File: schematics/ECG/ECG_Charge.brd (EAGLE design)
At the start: 100 x 80 mm, 8 parts, among them IC1 MCP73832_SOT23-5, J1 USB_MICROC

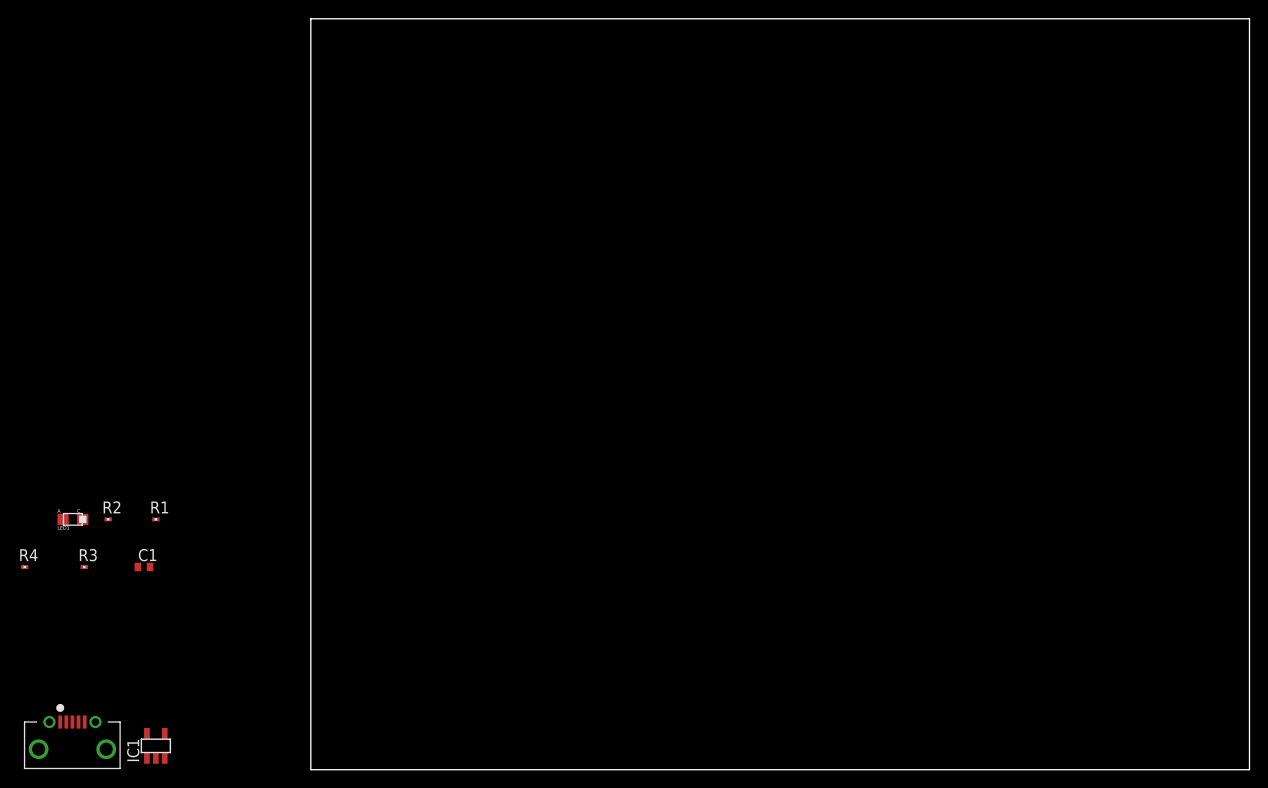
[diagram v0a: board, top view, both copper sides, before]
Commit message: changed usb to micro usb, placed components in board area
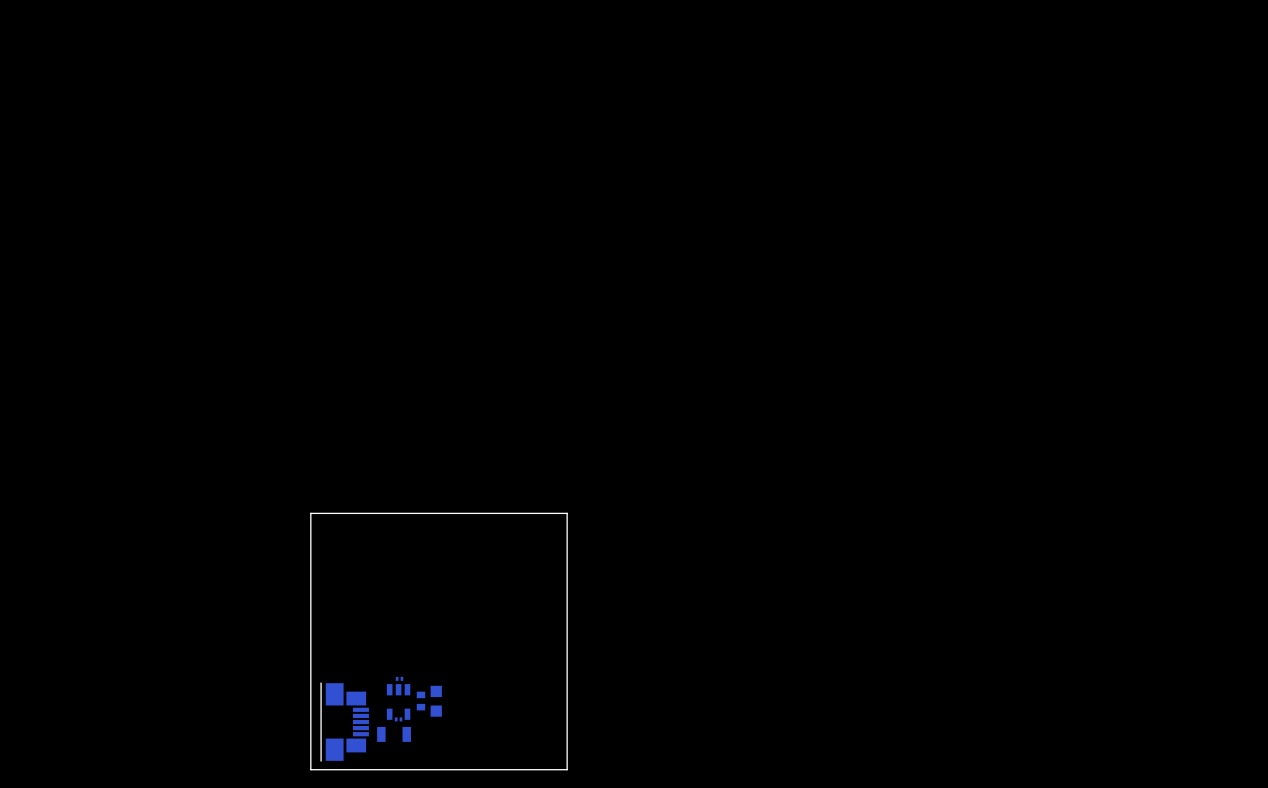
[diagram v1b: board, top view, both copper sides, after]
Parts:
- removed J1: USB_MICROC, KomodoOpenLab:USB_MICROB_FEMALE_RA_SMT
- removed R3, R4: 100K, rcl:R0201
- added FUSE: FUSE-MF_SERIES, bourns-fuse:1206
- added USBCONN: MOLEX-47346-0001, usb_con-update:MOLEX-47364-0001
- moved LED1 43.4 mm to (13.4, 7.24), flipped to the bottom, turned to 90 degrees
- moved R2 37.6 mm to (9.35, 5.36), flipped to the bottom
- moved C1 32.8 mm to (11.7, 7.32), flipped to the bottom, turned to 90 degrees
- moved R1 31.0 mm to (9.45, 9.68), flipped to the bottom, turned to 180 degrees
- moved IC1 26.3 mm to (9.35, 7.21), flipped to the bottom, turned to 180 degrees
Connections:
- removed net CHARGE_STAT: R3.1, R4.2
- removed net VIN: C1.1, IC1.4, J1.P$1, LED1.A
- new net VUSB: C1.1, FUSE.2, IC1.4, LED1.A
- new net VUSB_5V: FUSE.1, USBCONN.1
- net GND: now also USBCONN.5; no longer J1.P$5, R4.1
- net STAT: no longer R3.2
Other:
- board size 100 x 80 mm -> 27.3 x 27.3 mm
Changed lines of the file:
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@@
 <setting verticaltext="up"/>
 </settings>
-<grid distance="0.05" unitdist="inch" unit="inch" style="lines" multiple="1" display="no" altdistance="0.025" altunitdist="inch" altunit="inch"/>
+<grid distance="1" unitdist="mil" unit="mil" style="lines" multiple="1" display="no" altdistance="0.025" altunitdist="inch" altunit="inch"/>
 <layers>
 <layer number="1" name="Top" color="4" fill="1" visible="yes" active="yes"/>
+<layer number="2" name="Route2" color="1" fill="3" visible="no" active="no"/>
+<layer number="3" name="Route3" color="4" fill="3" visible="no" active="no"/>
+<layer number="14" name="Route14" color="1" fill="6" visible="no" active="no"/>
+<layer number="15" name="Route15" color="4" fill="6" visible="no" active="no"/>
 <layer number="16" name="Bottom" color="1" fill="1" visible="yes" active="yes"/>
 <layer number="17" name="Pads" color="2" fill="1" visible="yes" active="yes"/>
@@
 <board>
 <plain>
-<wire x1="0" y1="0" x2="100" y2="0" width="0" layer="20"/>
-<wire x1="100" y1="0" x2="100" y2="80" width="0" layer="20"/>
-<wire x1="100" y1="80" x2="0" y2="80" width="0" layer="20"/>
-<wire x1="0" y1="80" x2="0" y2="0" width="0" layer="20"/>
+<wire x1="0" y1="0" x2="27.305" y2="0" width="0" layer="20"/>
+<wire x1="27.305" y1="0" x2="27.305" y2="27.305" width="0" layer="20"/>
+<wire x1="27.305" y1="27.305" x2="0" y2="27.305" width="0" layer="20"/>
+<wire x1="0" y1="27.305" x2="0" y2="0" width="0" layer="20"/>
 </plain>
 <attributes>
@@
 </autorouter>
 <elements>
-<element name="J1" library="KomodoOpenLab" package="USB_MICROB_FEMALE_RA_SMT" value="USB_MICROC" x="-25.4" y="2.54">
-<attribute name="DIGIKEY" value="WM1399CT-ND" x="0" y="0" size="1.778" layer="27" display="off"/>
-<attribute name="PN" value="ZX62D-B-5PA8" x="0" y="0" size="1.778" layer="27" display="off"/>
-</element>
-<element name="IC1" library="KomodoOpenLab" package="SOT23-5" value="MCP73832_SOT23-5" x="-16.51" y="2.54"/>
-<element name="R2" library="rcl" package="R0201" value="10K" x="-21.59" y="26.67"/>
-<element name="C1" library="rcl" package="C0402" value="4.7uF" x="-17.78" y="21.59"/>
-<element name="R3" library="rcl" package="R0201" value="100K" x="-24.13" y="21.59"/>
-<element name="R4" library="rcl" package="R0201" value="100K" x="-30.48" y="21.59"/>
-<element name="LED1" library="LITEON" package="SMT_LED_0805" value="LED_SMT_0805" x="-25.4" y="26.67"/>
-<element name="R1" library="rcl" package="R0201" value="470" x="-16.51" y="26.67"/>
+<element name="IC1" library="KomodoOpenLab" package="SOT23-5" value="MCP73832_SOT23-5" x="9.3472" y="7.2136" rot="MR180"/>
+<element name="R2" library="rcl" package="R0201" value="10K" x="9.3472" y="5.3594" rot="MR0"/>
+<element name="C1" library="rcl" package="C0402" value="4.7uF" x="11.7348" y="7.3152" rot="MR90"/>
+<element name="LED1" library="LITEON" package="SMT_LED_0805" value="LED_SMT_0805" x="13.3604" y="7.239" rot="MR90"/>
+<element name="R1" library="rcl" package="R0201" value="470" x="9.4488" y="9.6774" rot="MR180"/>
+<element name="USBCONN" library="usb_con-update" package="MOLEX-47364-0001" value="MOLEX-47346-0001" x="2.54" y="5.08" rot="MR180"/>
+<element name="FUSE" library="bourns-fuse" package="1206" value="FUSE-MF_SERIES" x="8.8646" y="3.7592" rot="MR180"/>
 </elements>
 <signals>
 <signal name="GND">
-<contactref element="J1" pad="P$5"/>
 <contactref element="C1" pad="2"/>
 <contactref element="IC1" pad="2"/>
-<contactref element="R4" pad="1"/>
-<wire x1="-16.51" y1="1.234" x2="-24.1" y2="5.08" width="0" layer="19" extent="1-1"/>
-<wire x1="-30.735" y1="21.59" x2="-24.1" y2="5.08" width="0" layer="19" extent="1-1"/>
-<wire x1="-17.13" y1="21.59" x2="-30.735" y2="21.59" width="0" layer="19" extent="1-1"/>
+<contactref element="USBCONN" pad="5"/>
+<wire x1="9.3472" y1="8.5196" x2="11.7348" y2="7.9652" width="0" layer="19" extent="16-16"/>
+<wire x1="5.34" y1="6.38" x2="9.3472" y2="8.5196" width="0" layer="19" extent="16-16"/>
 </signal>
 <signal name="STAT">
 <contactref element="IC1" pad="1"/>
-<contactref element="R3" pad="2"/>
 <contactref element="R1" pad="1"/>
-<wire x1="-23.875" y1="21.59" x2="-17.46" y2="1.234" width="0" layer="19" extent="1-1"/>
-<wire x1="-16.765" y1="26.67" x2="-23.875" y2="21.59" width="0" layer="19" extent="1-1"/>
+<wire x1="9.1938" y1="9.6774" x2="8.3972" y2="8.5196" width="0" layer="19" extent="16-16"/>
 </signal>
 <signal name="VSS">
@@
 <contactref element="IC1" pad="5"/>
 <contactref element="R2" pad="2"/>
-<wire x1="-21.335" y1="26.67" x2="-17.46" y2="3.846" width="0" layer="19" extent="1-1"/>
-</signal>
-<signal name="VIN">
+<wire x1="9.0922" y1="5.3594" x2="8.3972" y2="5.9076" width="0" layer="19" extent="16-16"/>
+</signal>
+<signal name="BATT">
+<contactref element="IC1" pad="3"/>
+</signal>
+<signal name="N$3">
+<contactref element="LED1" pad="C"/>
+<contactref element="R1" pad="2"/>
+<wire x1="9.7038" y1="9.6774" x2="13.3604" y2="8.339" width="0" layer="19" extent="16-16"/>
+</signal>
+<signal name="VUSB">
 <contactref element="IC1" pad="4"/>
 <contactref element="C1" pad="1"/>
 <contactref element="LED1" pad="A"/>
-<contactref element="J1" pad="P$1"/>
-<wire x1="-15.56" y1="3.846" x2="-26.7" y2="5.08" width="0" layer="19" extent="1-1"/>
-<wire x1="-18.43" y1="21.59" x2="-15.56" y2="3.846" width="0" layer="19" extent="1-1"/>
-<wire x1="-26.4" y1="26.67" x2="-18.43" y2="21.59" width="0" layer="19" extent="1-1"/>
-</signal>
-<signal name="BATT">
-<contactref element="IC1" pad="3"/>
-</signal>
-<signal name="CHARGE_STAT">
-<contactref element="R3" pad="1"/>
-<contactref element="R4" pad="2"/>
-<wire x1="-24.385" y1="21.59" x2="-30.225" y2="21.59" width="0" layer="19" extent="1-1"/>
-</signal>
-<signal name="N$3">
-<contactref element="LED1" pad="C"/>
-<contactref element="R1" pad="2"/>
-<wire x1="-24.3" y1="26.67" x2="-16.255" y2="26.67" width="0" layer="19" extent="1-1"/>
+<contactref element="FUSE" pad="2"/>
+<wire x1="11.7348" y1="6.6652" x2="13.3604" y2="6.239" width="0" layer="19" extent="16-16"/>
+<wire x1="10.2972" y1="5.9076" x2="11.7348" y2="6.6652" width="0" layer="19" extent="16-16"/>
+<wire x1="10.2146" y1="3.7592" x2="10.2972" y2="5.9076" width="0" layer="19" extent="16-16"/>
+</signal>
+<signal name="VUSB_5V">
+<contactref element="USBCONN" pad="1"/>
+<contactref element="FUSE" pad="1"/>
+<wire x1="7.5146" y1="3.7592" x2="5.34" y2="3.78" width="0" layer="19" extent="16-16"/>
 </signal>
 </signals>
